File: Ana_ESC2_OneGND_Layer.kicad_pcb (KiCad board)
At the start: 4 copper layers, 90 x 90 mm, 104 parts, among them IC1 TCAN330DCNT, J1 BM04B-GHS-TBT_LF__SN__N_, J2 USB_C_Receptacle_USB2.0_16P, J3 Conn_01x02_Socket, J4 Conn_01x04_Pin, J5 BM04B-GHS-TBT_LF__SN__N_, Q10 STL90N6F7, Q11 STL90N6F7, Q12 STL90N6F7, Q7 STL90N6F7, Q8 STL90N6F7, Q9 STL90N6F7, SW1 SW_SPDT, SW2 SW_SPDT, U1 DRV8323RSRGZR, U2 ME6211C33M5, U3 STM32G431CBU6, Y1 ECS-80-20-5PX-TR

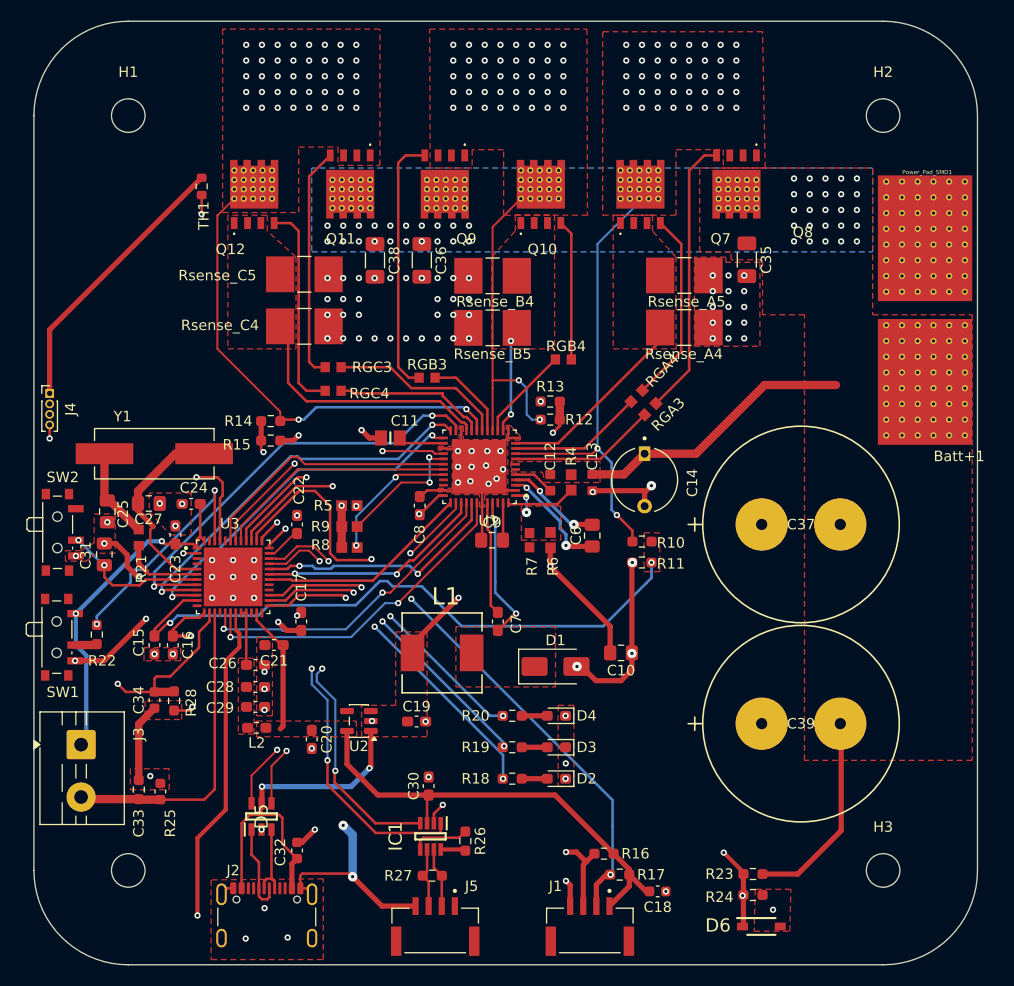
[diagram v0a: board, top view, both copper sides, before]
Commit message: some drc rule checks and correcting
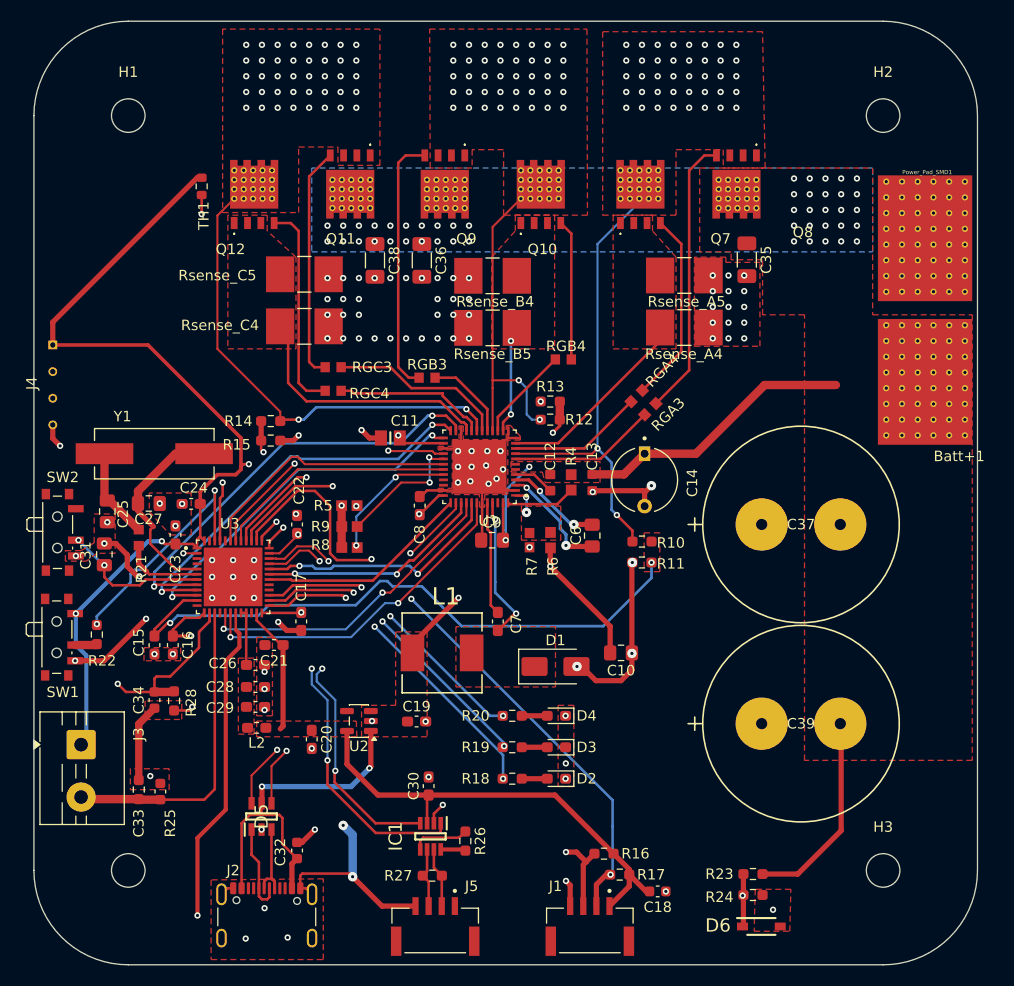
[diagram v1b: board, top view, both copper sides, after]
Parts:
- moved J4 5.55 mm to (50.3, 92.5)
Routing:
- net +3.3V: track 123.1 -> 173.8 mm, vias 2 -> 5
- net GND2: track 55.3 -> 64.6 mm
- net VM: track 49.8 -> 57.7 mm, vias 45 -> 47
- net /Gate_Driver/SENS3: track 20.5 -> 24.0 mm
- net /MCU/VBus: track 91.6 -> 88.9 mm, vias 3 -> 2
- net /MCU/SWDIO: track 30.4 -> 31.2 mm
- net /Gate_Driver/SENS2: track 58.3 -> 57.5 mm
- net GND: vias 67 -> 68

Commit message: minor rule checking warning
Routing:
- net +3.3V: track 173.8 -> 186.1 mm, vias 5 -> 6
- net /Gate_Driver/SENS3: track 24.0 -> 23.4 mm
- net /Gate_Driver/SOB: track 38.7 -> 39.2 mm

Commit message: minor rule checking warning
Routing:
- added copper zone on B.Cu, net /Gate_Driver/SHA
- added copper zone on B.Cu, net /Gate_Driver/SHB
- added copper zone on B.Cu, net /Gate_Driver/SHC
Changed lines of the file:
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@@
 			(at 0.25 2.466 0)
 			(layer "F.SilkS")
+			(hide yes)
 			(effects
 				(font
@@
 		(at 99 83.76)
 		(property "Reference" "RGB4"
-			(at 0.25 -1.26 0)
+			(at 1.14 -1.54 0)
 			(layer "F.SilkS")
 			(effects
@@
 			(at 8.3008 -0.1138 0)
 			(layer "F.SilkS")
+			(hide yes)
 			(effects
 				(font
@@
 			(at -0.2082 -2.5 0)
 			(layer "F.SilkS")
+			(hide yes)
 			(effects
 				(font
@@
 		(tags "Diode")
 		(property "Reference" "D5"
-			(at -0.01 -2.95 90)
+			(at 0.01 -3.11 90)
 			(layer "F.SilkS")
 			(effects
@@
 			(at 0.0518 -2.764 0)
 			(layer "F.SilkS")
+			(hide yes)
 			(effects
 				(font
@@
 			(at 8.0508 0.1022 0)
 			(layer "F.SilkS")
+			(hide yes)
 			(effects
 				(font
@@
 			(at 0 2.5 0)
 			(layer "F.SilkS")
+			(hide yes)
 			(effects
 				(font
@@
 			)
 		)
+	)
+	(zone
+		(net 45)
+		(net_name "/Gate_Driver/SHC")
+		(layer "B.Cu")
+		(hatch edge 0.5)
+		(priority 24)
+		(connect_pads
+			(clearance 0.3)
+		)
+		(min_thickness 0.25)
+		(filled_areas_thickness no)
+		(fill yes
+			(thermal_gap 0.5)
+			(thermal_bridge_width 0.5)
+		)
+		(polygon
+			(pts
+				(xy 66.221733 52.495645) (xy 66.091733 61.865645) (xy 81.781733 61.735645) (xy 81.471733 52.495645)
+			)
+		)
+	)
+	(zone
+		(net 38)
+		(net_name "/Gate_Driver/SHA")
+		(layer "B.Cu")
+		(hatch edge 0.5)
+		(priority 24)
+		(connect_pads
+			(clearance 0.3)
+		)
+		(min_thickness 0.25)
+		(filled_areas_thickness no)
+		(fill yes
+			(thermal_gap 0.5)
+			(thermal_bridge_width 0.5)
+		)
+		(polygon
+			(pts
+				(xy 102.718651 52.489091) (xy 102.588651 61.859091) (xy 118.278651 61.729091) (xy 117.968651 52.489091)
+			)
+		)
+	)
+	(zone
+		(net 41)
+		(net_name "/Gate_Driver/SHB")
+		(layer "B.Cu")
+		(hatch edge 0.5)
+		(priority 24)
+		(connect_pads
+			(clearance 0.3)
+		)
+		(min_thickness 0.25)
+		(filled_areas_thickness no)
+		(fill yes
+			(thermal_gap 0.5)
+			(thermal_bridge_width 0.5)
+		)
+		(polygon
+			(pts
+				(xy 86.208029 52.494006) (xy 86.078029 61.864006) (xy 101.768029 61.734006) (xy 101.458029 52.494006)
+			)
+		)
